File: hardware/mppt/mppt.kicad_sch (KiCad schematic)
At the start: 4 parts

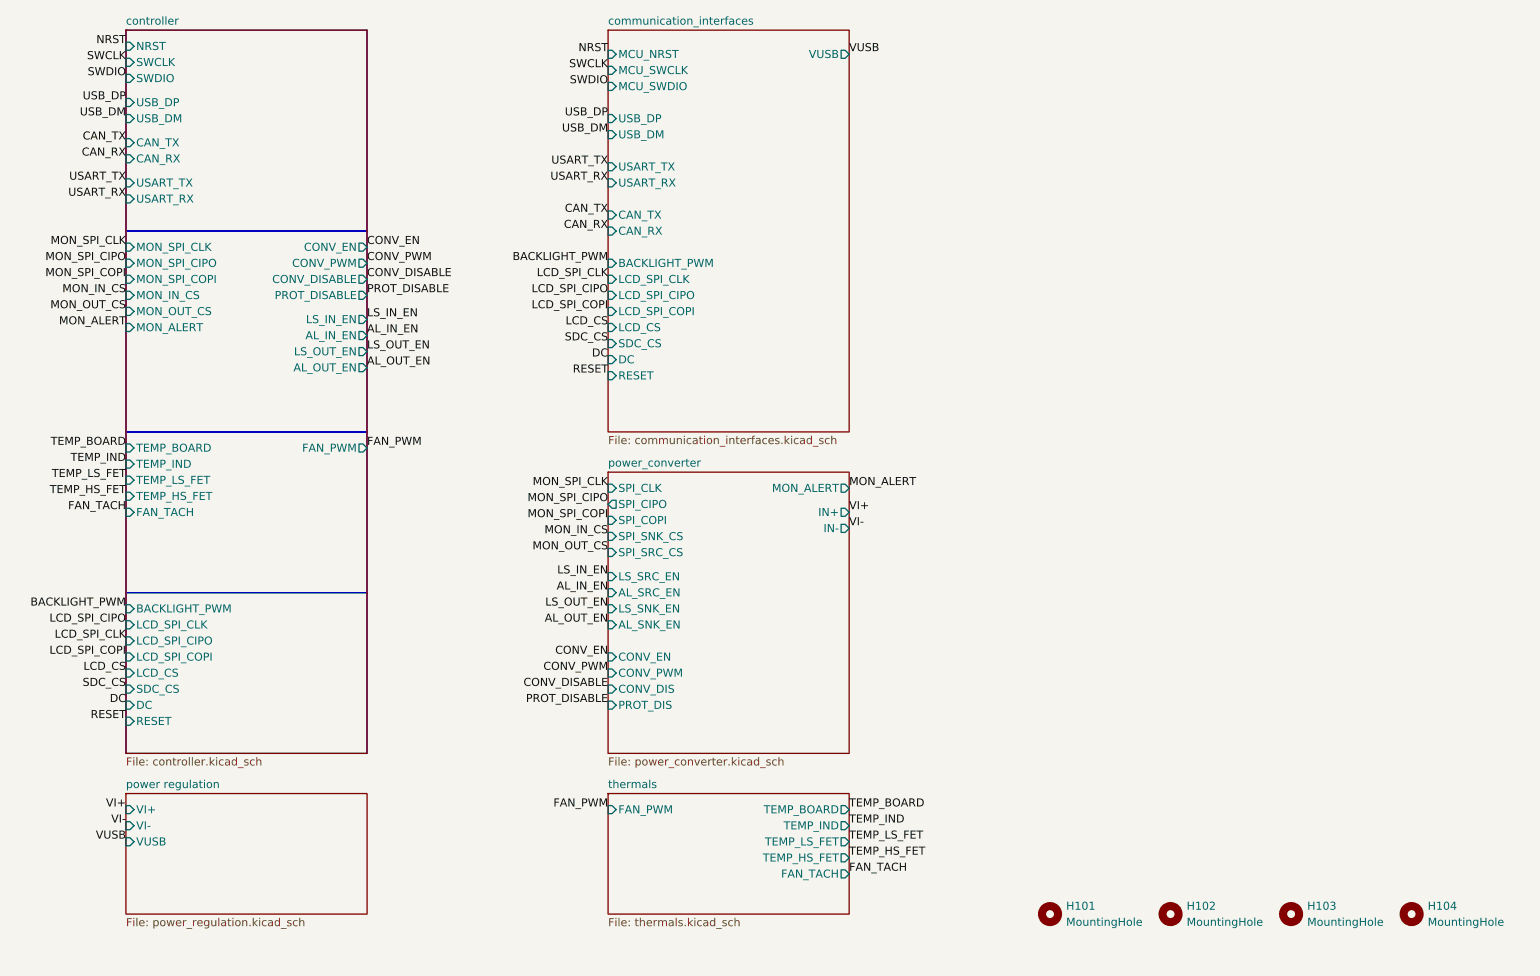
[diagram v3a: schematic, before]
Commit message: complete layout, drc, signaling optimizations and added dnp testpoints
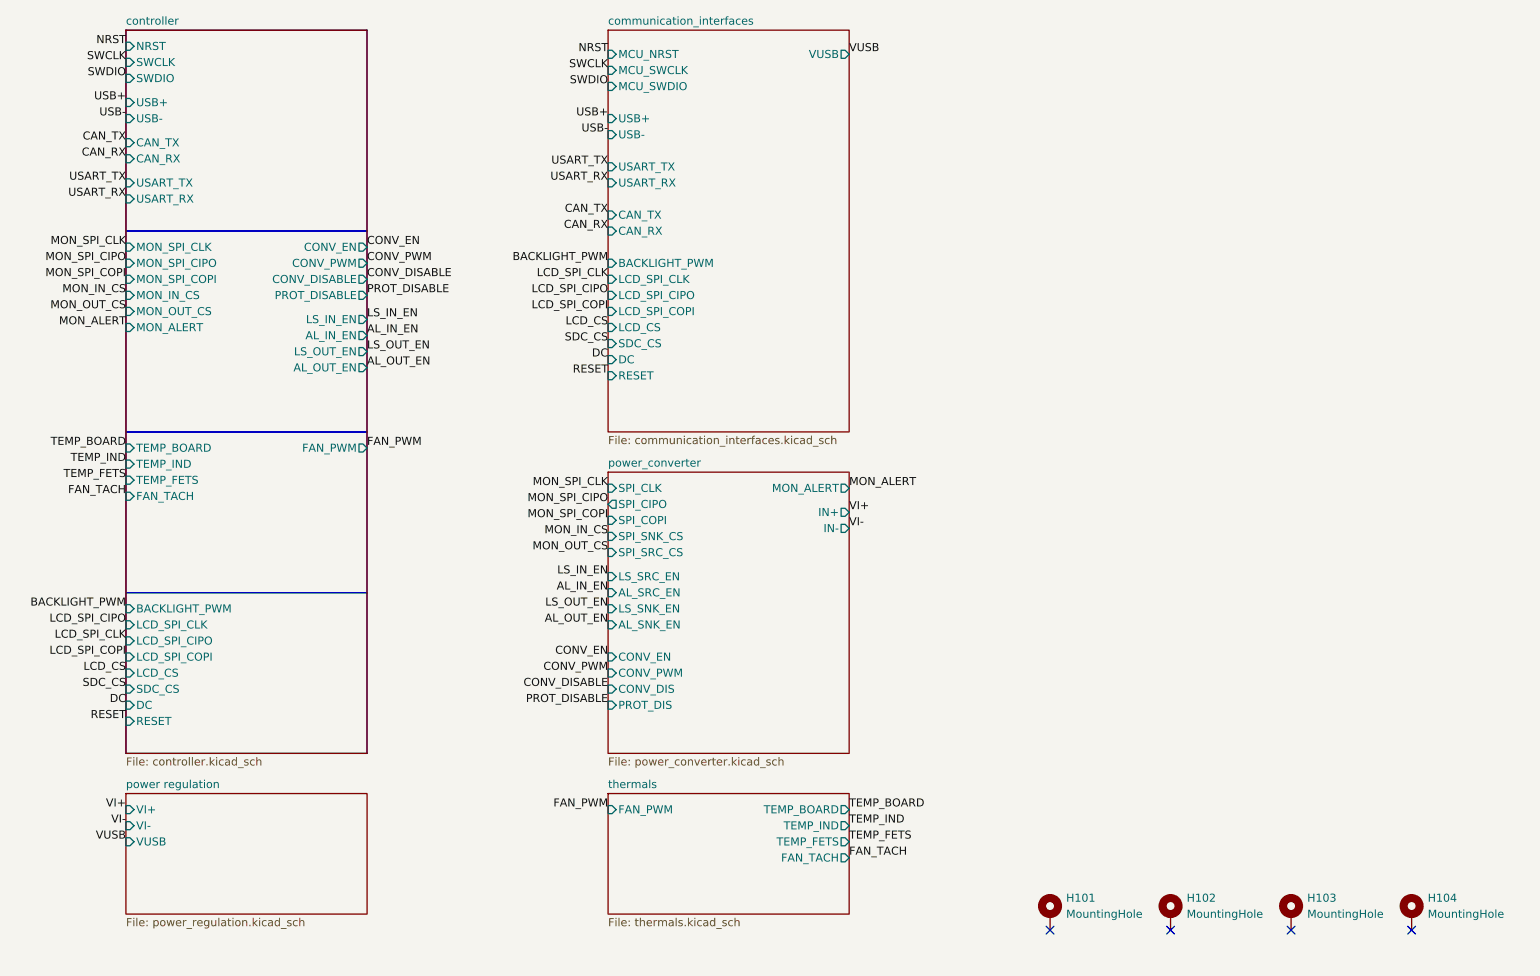
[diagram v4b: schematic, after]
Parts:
- H101, H102, H103, H104: symbol Mechanical:MountingHole -> Mechanical:MountingHole_Pad
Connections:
- no-connect marks 0 -> 4
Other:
- sheet communication_interfaces ports: added USB+, USB-; removed USB_DM, USB_DP
- sheet controller ports: added TEMP_FETS, USB+, USB-; removed TEMP_HS_FET, TEMP_LS_FET, USB_DM, USB_DP
- sheet thermals ports: added TEMP_FETS; removed TEMP_HS_FET, TEMP_LS_FET
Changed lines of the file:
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@@
 		(comment 2 "Jacob Pustilnik")
+	)
+	(no_connect
+		(at 222.25 167.64)
+	)
+	(no_connect
+		(at 184.15 167.64)
+	)
+	(no_connect
+		(at 241.3 167.64)
+	)
+	(no_connect
+		(at 203.2 167.64)
 	)
 	(rectangle
@@
 	)
 	(label "FAN_TACH"
-		(at 152.4 158.75 0)
+		(at 152.4 156.21 0)
 		(fields_autoplaced yes)
 		(effects
@@
 		)
 	)
-	(label "TEMP_LS_FET"
+	(label "TEMP_FETS"
 		(at 152.4 153.67 0)
 		(fields_autoplaced yes)
@@
 		)
 	)
-	(label "TEMP_HS_FET"
-		(at 38.1 99.06 180)
-		(fields_autoplaced yes)
-		(effects
-			(font
-				(size 1.27 1.27)
-			)
-			(justify right bottom)
-		)
-	)
 	(label "PROT_DISABLE"
 		(at 76.2 67.31 0)
@@
 		)
 	)
-	(label "USB_DM"
+	(label "USB-"
 		(at 114.3 41.91 180)
 		(fields_autoplaced yes)
@@
 		)
 	)
-	(label "USB_DP"
+	(label "USB+"
 		(at 114.3 39.37 180)
 		(fields_autoplaced yes)
@@
 		)
 	)
-	(label "USB_DM"
+	(label "USB-"
 		(at 38.1 39.37 180)
 		(fields_autoplaced yes)
@@
 		)
 	)
-	(label "TEMP_HS_FET"
-		(at 152.4 156.21 0)
-		(fields_autoplaced yes)
-		(effects
-			(font
-				(size 1.27 1.27)
-			)
-			(justify left bottom)
-		)
-	)
 	(label "CAN_TX"
 		(at 38.1 43.18 180)
@@
 		)
 	)
-	(label "USB_DP"
+	(label "USB+"
 		(at 38.1 36.83 180)
 		(fields_autoplaced yes)
@@
 	)
 	(label "FAN_TACH"
-		(at 38.1 101.6 180)
+		(at 38.1 99.06 180)
 		(fields_autoplaced yes)
 		(effects
@@
 		)
 	)
-	(label "TEMP_LS_FET"
-		(at 38.1 96.52 180)
-		(fields_autoplaced yes)
-		(effects
-			(font
-				(size 1.27 1.27)
-			)
-			(justify right bottom)
-		)
-	)
 	(label "MON_SPI_CLK"
 		(at 38.1 59.69 180)
@@
 		)
 	)
+	(label "TEMP_FETS"
+		(at 38.1 96.52 180)
+		(fields_autoplaced yes)
+		(effects
+			(font
+				(size 1.27 1.27)
+			)
+			(justify right bottom)
+		)
+	)
 	(label "LCD_SPI_COPI"
 		(at 114.3 69.85 180)
@@
 	)
 	(symbol
-		(lib_id "Mechanical:MountingHole")
+		(lib_id "Mechanical:MountingHole_Pad")
 		(at 222.25 165.1 0)
 		(unit 1)
-		(exclude_from_sim no)
+		(exclude_from_sim yes)
 		(in_bom no)
 		(on_board yes)
@@
 		(fields_autoplaced yes)
 		(property "Reference" "H103"
-			(at 224.79 163.8299 0)
+			(at 224.79 162.5599 0)
 			(effects
 				(font
@@
 		)
 		(property "Value" "MountingHole"
-			(at 224.79 166.3699 0)
+			(at 224.79 165.0999 0)
 			(effects
 				(font
@@
 			)
 		)
-		(property "Datasheet" ""
+		(property "Datasheet" "~"
 			(at 222.25 165.1 0)
 			(effects
@@
 			)
 		)
-		(property "Description" "Mounting Hole without connection"
+		(property "Description" "Mounting Hole with connection"
 			(at 222.25 165.1 0)
 			(effects
@@
 				(hide yes)
 			)
+		)
+		(pin "1"
 		)
 		(instances
@@
 	)
 	(symbol
-		(lib_id "Mechanical:MountingHole")
+		(lib_id "Mechanical:MountingHole_Pad")
 		(at 184.15 165.1 0)
 		(unit 1)
-		(exclude_from_sim no)
+		(exclude_from_sim yes)
 		(in_bom no)
 		(on_board yes)
@@
 		(fields_autoplaced yes)
 		(property "Reference" "H101"
-			(at 186.69 163.8299 0)
+			(at 186.69 162.5599 0)
 			(effects
 				(font
@@
 		)
 		(property "Value" "MountingHole"
-			(at 186.69 166.3699 0)
+			(at 186.69 165.0999 0)
 			(effects
 				(font
@@
 			)
 		)
-		(property "Datasheet" ""
+		(property "Datasheet" "~"
 			(at 184.15 165.1 0)
 			(effects
@@
 			)
 		)
-		(property "Description" "Mounting Hole without connection"
+		(property "Description" "Mounting Hole with connection"
 			(at 184.15 165.1 0)
 			(effects
@@
 				(hide yes)
 			)
+		)
+		(pin "1"
 		)
 		(instances
@@
 	)
 	(symbol
-		(lib_id "Mechanical:MountingHole")
+		(lib_id "Mechanical:MountingHole_Pad")
 		(at 241.3 165.1 0)
 		(unit 1)
-		(exclude_from_sim no)
+		(exclude_from_sim yes)
 		(in_bom no)
 		(on_board yes)
@@
 		(fields_autoplaced yes)
 		(property "Reference" "H104"
-			(at 243.84 163.8299 0)
+			(at 243.84 162.5599 0)
 			(effects
 				(font
@@
 		)
 		(property "Value" "MountingHole"
-			(at 243.84 166.3699 0)
+			(at 243.84 165.0999 0)
 			(effects
 				(font
@@
 			)
 		)
-		(property "Datasheet" ""
+		(property "Datasheet" "~"
 			(at 241.3 165.1 0)
 			(effects
@@
 			)
 		)
-		(property "Description" "Mounting Hole without connection"
+		(property "Description" "Mounting Hole with connection"
 			(at 241.3 165.1 0)
 			(effects
@@
 				(hide yes)
 			)
+		)
+		(pin "1"
 		)
 		(instances
@@
 	)
 	(symbol
-		(lib_id "Mechanical:MountingHole")
+		(lib_id "Mechanical:MountingHole_Pad")
 		(at 203.2 165.1 0)
 		(unit 1)
-		(exclude_from_sim no)
+		(exclude_from_sim yes)
 		(in_bom no)
 		(on_board yes)
@@
 		(fields_autoplaced yes)
 		(property "Reference" "H102"
-			(at 205.74 163.8299 0)
+			(at 205.74 162.5599 0)
 			(effects
 				(font
@@
 		)
 		(property "Value" "MountingHole"
-			(at 205.74 166.3699 0)
+			(at 205.74 165.0999 0)
 			(effects
 				(font
@@
 			)
 		)
-		(property "Datasheet" ""
+		(property "Datasheet" "~"
 			(at 203.2 165.1 0)
 			(effects
@@
 			)
 		)
-		(property "Description" "Mounting Hole without connection"
+		(property "Description" "Mounting Hole with connection"
 			(at 203.2 165.1 0)
 			(effects
@@
 				(hide yes)
 			)
+		)
+		(pin "1"
 		)
 		(instances
@@
 			)
 		)
-		(pin "TEMP_HS_FET" input
-			(at 38.1 99.06 180)
-			(effects
-				(font
-					(size 1.27 1.27)
-				)
-				(justify left)
-			)
-		)
-		(pin "TEMP_LS_FET" input
+		(pin "TEMP_FETS" input
 			(at 38.1 96.52 180)
 			(effects
@@
 			)
 		)
-		(pin "USB_DM" input
+		(pin "USB-" input
 			(at 38.1 39.37 180)
 			(effects
@@
 			)
 		)
-		(pin "USB_DP" input
+		(pin "USB+" input
 			(at 38.1 36.83 180)
 			(effects
@@
 		)
 		(pin "FAN_TACH" input
-			(at 38.1 101.6 180)
+			(at 38.1 99.06 180)
 			(effects
 				(font
@@
 			)
 		)
-		(pin "TEMP_LS_FET" output
-			(at 152.4 153.67 0)
-			(effects
-				(font
-					(size 1.27 1.27)
-				)
-				(justify right)
-			)
-		)
-		(pin "TEMP_HS_FET" output
-			(at 152.4 156.21 0)
-			(effects
-				(font
-					(size 1.27 1.27)
-				)
-				(justify right)
-			)
-		)
 		(pin "TEMP_IND" output
 			(at 152.4 151.13 0)
@@
 		)
 		(pin "FAN_TACH" output
-			(at 152.4 158.75 0)
+			(at 152.4 156.21 0)
+			(effects
+				(font
+					(size 1.27 1.27)
+				)
+				(justify right)
+			)
+		)
+		(pin "TEMP_FETS" output
+			(at 152.4 153.67 0)
 			(effects
 				(font
@@
 			)
 		)
-		(pin "USB_DP" input
+		(pin "USB+" input
 			(at 114.3 39.37 180)
 			(effects
@@
 			)
 		)
-		(pin "USB_DM" input
+		(pin "USB-" input
 			(at 114.3 41.91 180)
 			(effects

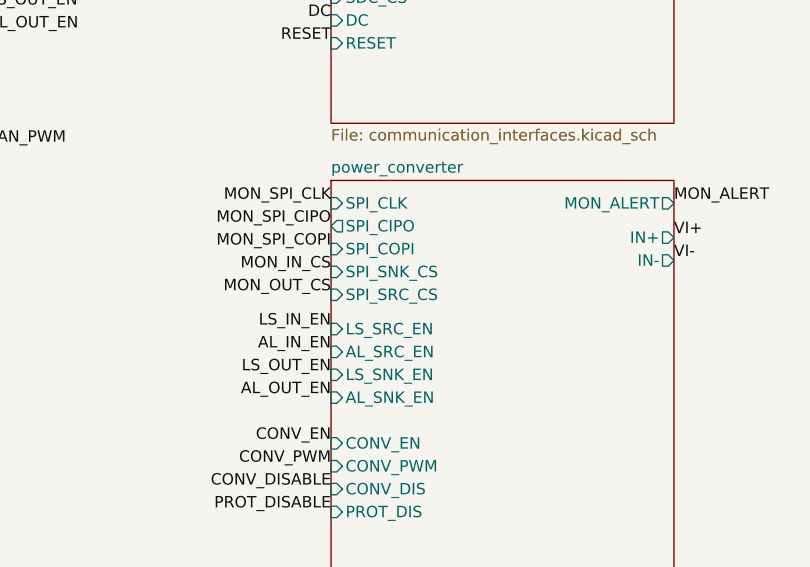
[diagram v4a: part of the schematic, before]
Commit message: converter schematic and layout.
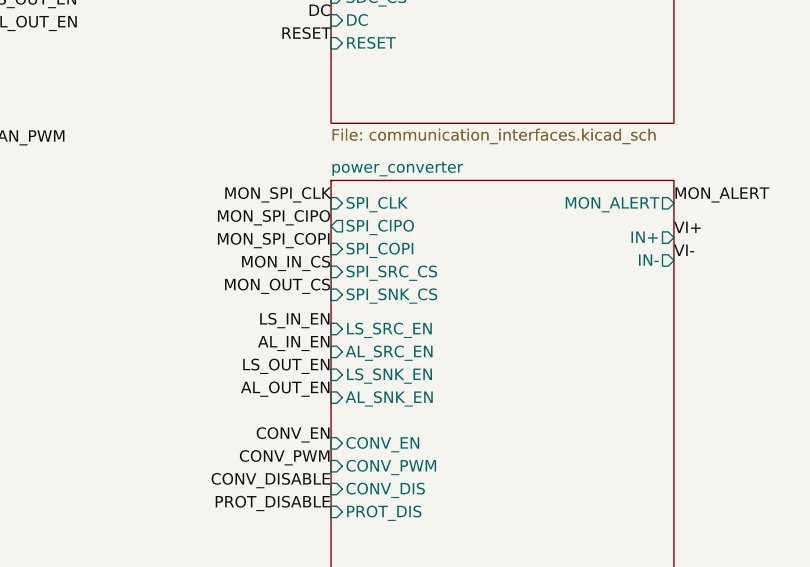
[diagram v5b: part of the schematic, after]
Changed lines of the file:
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@@
+		)
+	)
+	(label "NRST"
+		(at 38.1 27.94 180)
+		(fields_autoplaced yes)
+		(effects
+			(font
+				(size 1.27 1.27)
+			)
+			(justify right bottom)
+		)
+	)
+	(label "CONV_PWM"
+		(at 114.3 127 180)
+		(fields_autoplaced yes)
+		(effects
+			(font
+				(size 1.27 1.27)
+			)
+			(justify right bottom)
+		)
+	)
+	(label "USART_RX"
+		(at 38.1 52.07 180)
+		(fields_autoplaced yes)
+		(effects
+			(font
+				(size 1.27 1.27)
+			)
+			(justify right bottom)
+		)
+	)
+	(label "LS_OUT_EN"
+		(at 76.2 76.2 0)
+		(fields_autoplaced yes)
+		(effects
+			(font
+				(size 1.27 1.27)
+			)
+			(justify left bottom)
+		)
+	)
+	(label "MON_SPI_CIPO"
+		(at 114.3 100.33 180)
+		(fields_autoplaced yes)
+		(effects
+			(font
+				(size 1.27 1.27)
+			)
+			(justify right bottom)
+		)
+	)
+	(label "DC"
+		(at 38.1 132.08 180)
+		(fields_autoplaced yes)
+		(effects
+			(font
+				(size 1.27 1.27)
+			)
+			(justify right bottom)
+		)
+	)
+	(label "USB+"
+		(at 114.3 39.37 180)
+		(fields_autoplaced yes)
+		(effects
+			(font
+				(size 1.27 1.27)
+			)
+			(justify right bottom)
+		)
+	)
+	(label "LCD_CS"
+		(at 38.1 127 180)
+		(fields_autoplaced yes)
+		(effects
+			(font
+				(size 1.27 1.27)
+			)
+			(justify right bottom)
+		)
+	)
+	(label "CONV_DISABLE"
+		(at 114.3 129.54 180)
+		(fields_autoplaced yes)
+		(effects
+			(font
+				(size 1.27 1.27)
+			)
+			(justify right bottom)
+		)
+	)
+	(label "PROT_DISABLE"
+		(at 114.3 132.08 180)
+		(fields_autoplaced yes)
+		(effects
+			(font
+				(size 1.27 1.27)
+			)
+			(justify right bottom)
+		)
+	)
+	(label "DC"
+		(at 114.3 77.47 180)
+		(fields_autoplaced yes)
+		(effects
+			(font
+				(size 1.27 1.27)
+			)
+			(justify right bottom)
+		)
+	)
+	(label "BACKLIGHT_PWM"
+		(at 114.3 62.23 180)
+		(fields_autoplaced yes)
+		(effects
+			(font
+				(size 1.27 1.27)
+			)
+			(justify right bottom)
+		)
+	)
+	(label "RESET"
+		(at 114.3 80.01 180)
+		(fields_autoplaced yes)
+		(effects
+			(font
+				(size 1.27 1.27)
+			)
+			(justify right bottom)
+		)
+	)
+	(label "MON_SPI_COPI"
+		(at 114.3 102.87 180)
+		(fields_autoplaced yes)
+		(effects
+			(font
+				(size 1.27 1.27)
+			)
+			(justify right bottom)
 		)
 	)
@@
 		)
 	)
+	(label "USB-"
+		(at 38.1 39.37 180)
+		(fields_autoplaced yes)
+		(effects
+			(font
+				(size 1.27 1.27)
+			)
+			(justify right bottom)
+		)
+	)
+	(label "CONV_EN"
+		(at 76.2 59.69 0)
+		(fields_autoplaced yes)
+		(effects
+			(font
+				(size 1.27 1.27)
+			)
+			(justify left bottom)
+		)
+	)
 	(label "MON_IN_CS"
 		(at 114.3 105.41 180)
@@
 			)
 			(justify right bottom)
-		)
-	)
-	(label "NRST"
-		(at 38.1 27.94 180)
-		(fields_autoplaced yes)
-		(effects
-			(font
-				(size 1.27 1.27)
-			)
-			(justify right bottom)
-		)
-	)
-	(label "CONV_PWM"
-		(at 114.3 127 180)
-		(fields_autoplaced yes)
-		(effects
-			(font
-				(size 1.27 1.27)
-			)
-			(justify right bottom)
-		)
-	)
-	(label "USART_RX"
-		(at 38.1 52.07 180)
-		(fields_autoplaced yes)
-		(effects
-			(font
-				(size 1.27 1.27)
-			)
-			(justify right bottom)
-		)
-	)
-	(label "LS_OUT_EN"
-		(at 76.2 76.2 0)
-		(fields_autoplaced yes)
-		(effects
-			(font
-				(size 1.27 1.27)
-			)
-			(justify left bottom)
-		)
-	)
-	(label "MON_SPI_CIPO"
-		(at 114.3 100.33 180)
-		(fields_autoplaced yes)
-		(effects
-			(font
-				(size 1.27 1.27)
-			)
-			(justify right bottom)
-		)
-	)
-	(label "DC"
-		(at 38.1 132.08 180)
-		(fields_autoplaced yes)
-		(effects
-			(font
-				(size 1.27 1.27)
-			)
-			(justify right bottom)
-		)
-	)
-	(label "USB+"
-		(at 114.3 39.37 180)
-		(fields_autoplaced yes)
-		(effects
-			(font
-				(size 1.27 1.27)
-			)
-			(justify right bottom)
-		)
-	)
-	(label "LCD_CS"
-		(at 38.1 127 180)
-		(fields_autoplaced yes)
-		(effects
-			(font
-				(size 1.27 1.27)
-			)
-			(justify right bottom)
-		)
-	)
-	(label "CONV_DISABLE"
-		(at 114.3 129.54 180)
-		(fields_autoplaced yes)
-		(effects
-			(font
-				(size 1.27 1.27)
-			)
-			(justify right bottom)
-		)
-	)
-	(label "PROT_DISABLE"
-		(at 114.3 132.08 180)
-		(fields_autoplaced yes)
-		(effects
-			(font
-				(size 1.27 1.27)
-			)
-			(justify right bottom)
-		)
-	)
-	(label "DC"
-		(at 114.3 77.47 180)
-		(fields_autoplaced yes)
-		(effects
-			(font
-				(size 1.27 1.27)
-			)
-			(justify right bottom)
-		)
-	)
-	(label "BACKLIGHT_PWM"
-		(at 114.3 62.23 180)
-		(fields_autoplaced yes)
-		(effects
-			(font
-				(size 1.27 1.27)
-			)
-			(justify right bottom)
-		)
-	)
-	(label "RESET"
-		(at 114.3 80.01 180)
-		(fields_autoplaced yes)
-		(effects
-			(font
-				(size 1.27 1.27)
-			)
-			(justify right bottom)
-		)
-	)
-	(label "MON_SPI_COPI"
-		(at 114.3 102.87 180)
-		(fields_autoplaced yes)
-		(effects
-			(font
-				(size 1.27 1.27)
-			)
-			(justify right bottom)
-		)
-	)
-	(label "USB-"
-		(at 38.1 39.37 180)
-		(fields_autoplaced yes)
-		(effects
-			(font
-				(size 1.27 1.27)
-			)
-			(justify right bottom)
-		)
-	)
-	(label "CONV_EN"
-		(at 76.2 59.69 0)
-		(fields_autoplaced yes)
-		(effects
-			(font
-				(size 1.27 1.27)
-			)
-			(justify left bottom)
 		)
 	)
@@
 		)
 		(pin "SPI_SNK_CS" input
-			(at 114.3 105.41 180)
+			(at 114.3 107.95 180)
 			(effects
 				(font
@@
 		)
 		(pin "SPI_SRC_CS" input
-			(at 114.3 107.95 180)
-			(effects
-				(font
+			(at 114.3 105.41 180)
+			(effects
+				(font
